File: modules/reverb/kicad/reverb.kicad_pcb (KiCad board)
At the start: 2 copper layers, 58.9 x 89.1 mm, 69 parts, among them P1 CONN_01X02, P2 CONN_01X03, P3 CONN_01X02, P4 CONN_01X03, P5 CONN_01X03, P6 CONN_01X02, P7 CONN_01X02, P8 CONN_01X02, P9 CONN_01X02, Q1 2N3906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

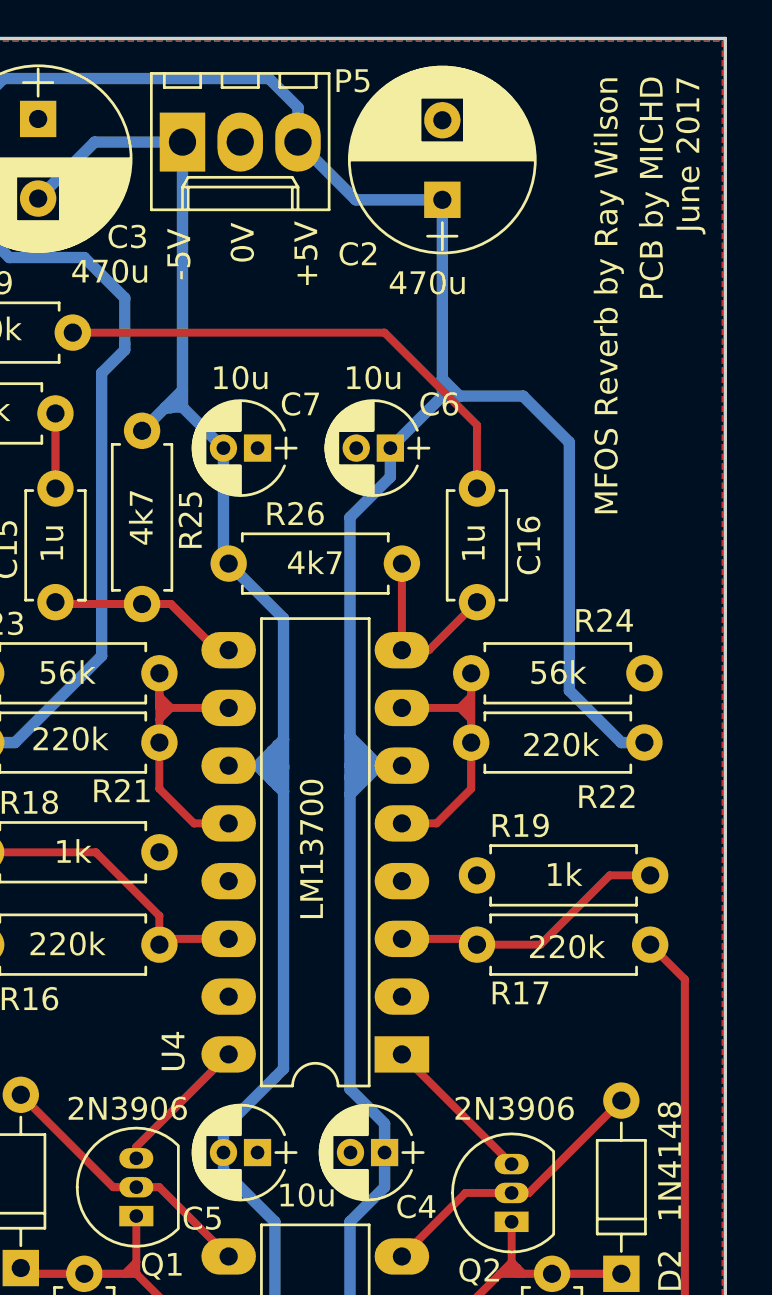
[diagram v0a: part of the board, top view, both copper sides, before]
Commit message: Reverb: Fix LM13700 power connections inverted
The power pins on the LM13700 OTA were the wrong way around. This causes
the LM13700 to, well, break. it'll heat up a bit and of course not
function.
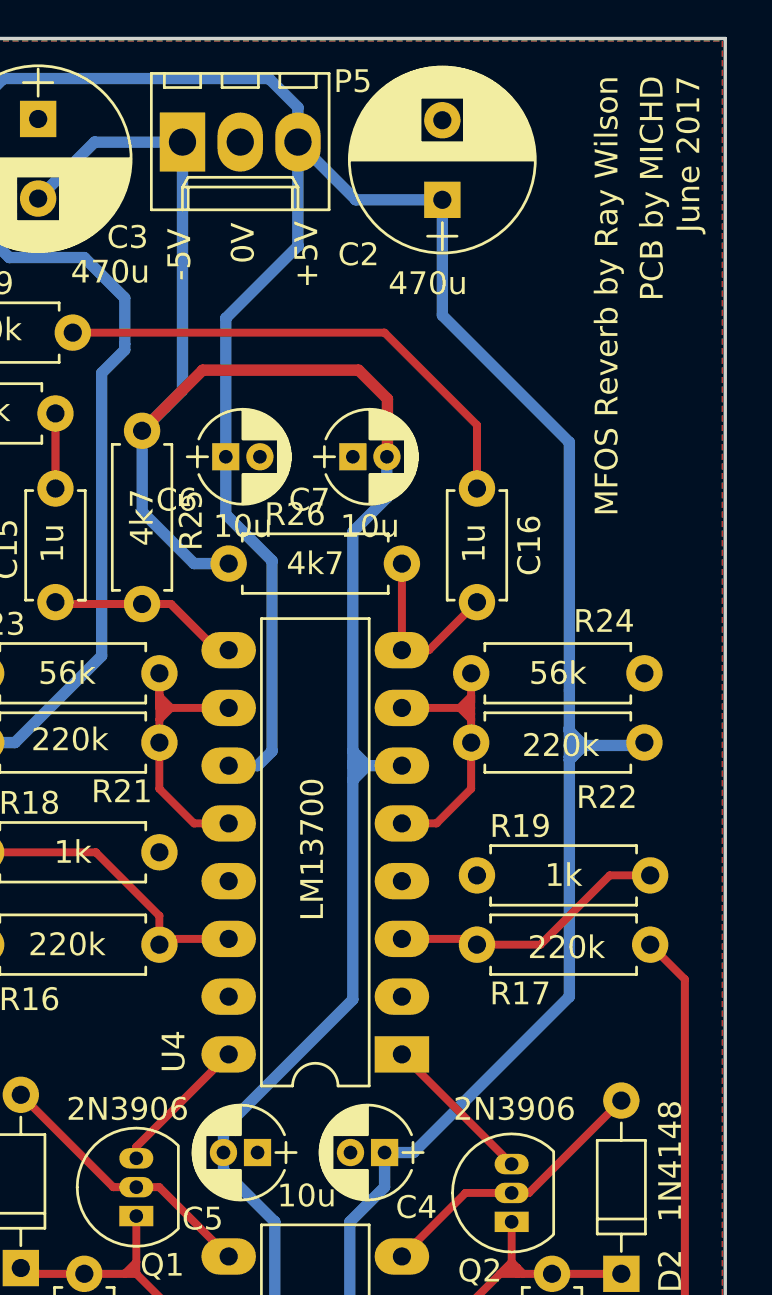
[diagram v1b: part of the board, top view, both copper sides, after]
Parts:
- moved C6 7.25 mm to (152.9, 64.3), turned to 0 degrees
- moved C7 4.21 mm to (158.5, 64.3), turned to 0 degrees
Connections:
- U4 pad 11: VEE -> VCC
- U4 pad 6: VCC -> VEE
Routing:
- net VEE: track 170.8 -> 185.5 mm
- net VCC: track 263.5 -> 271.0 mm
